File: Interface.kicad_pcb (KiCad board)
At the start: 4 copper layers, 126.6 x 95.8 mm, 92 parts, among them J101 AudioJack4, J102 switch, J3 TYPE-C-31-M-12, J4 CONN_DISPLAY, Q1 2N7002VC-7, Q2 2N7002VC-7, U1 W25Q128JVPIQ, U2 RP2040, U3 XC6210B332MR-G, Y1 12MHz

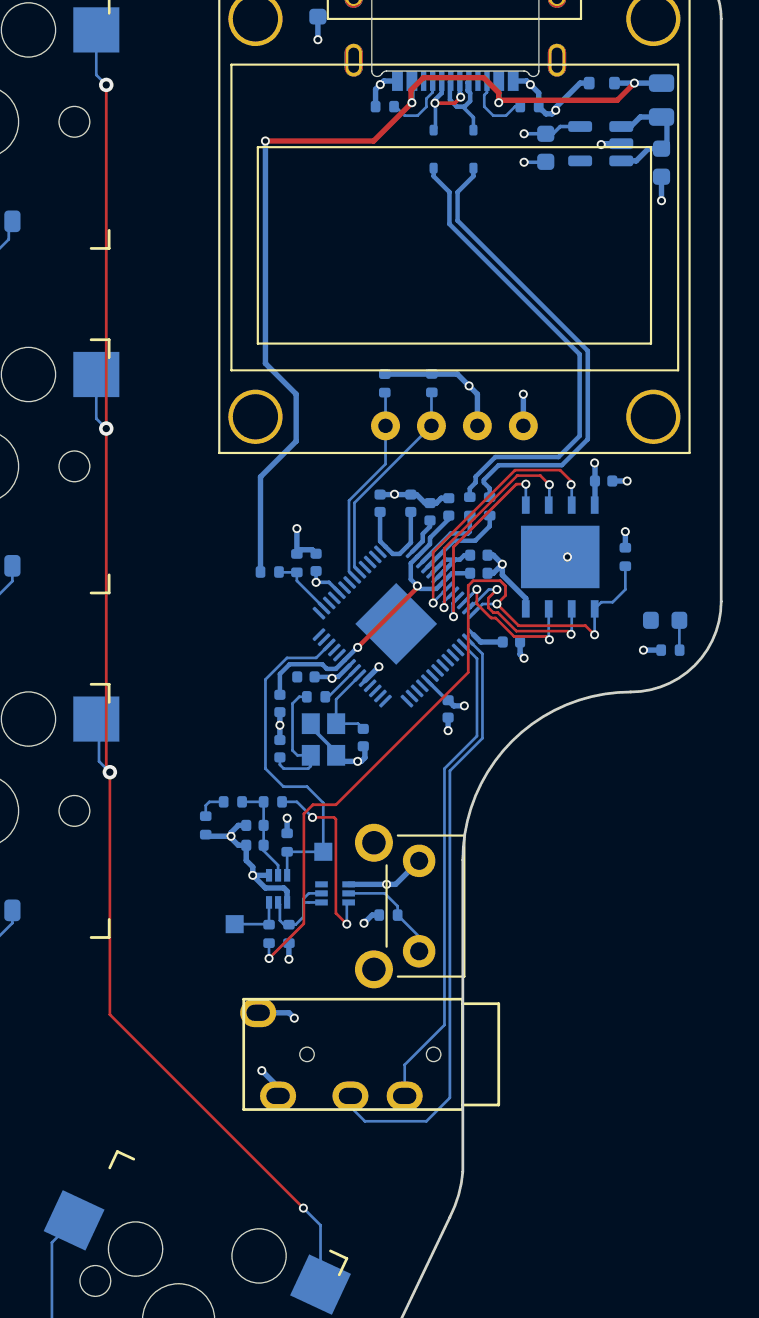
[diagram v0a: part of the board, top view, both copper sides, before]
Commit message: Add mounting holes
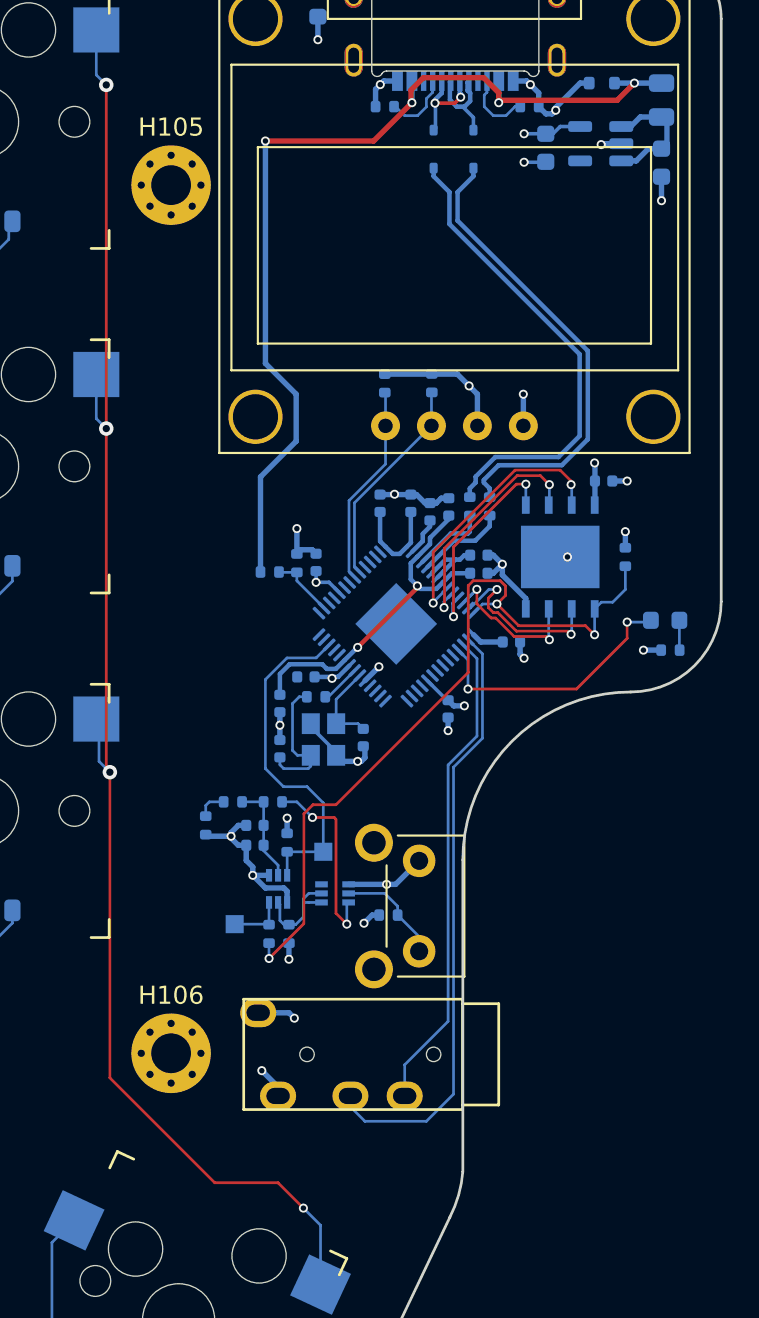
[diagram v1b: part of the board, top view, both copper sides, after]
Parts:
- added H105: MountingHole_Pad, MountingHole:MountingHole_2.2mm_M2_Pad_Via, F.Cu at (118.6, 50.9)
- added H106: MountingHole_Pad, MountingHole:MountingHole_2.2mm_M2_Pad_Via, F.Cu at (118.6, 98.9)
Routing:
- net /Left MCU/LED: track 0.00 -> 14.6 mm, vias 0 -> 2
- net /Left MCU/COL-5: track 79.7 -> 81.8 mm
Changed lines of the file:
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@@
     )
   )
+  (footprint "MountingHole:MountingHole_2.2mm_M2_Pad_Via" (layer "F.Cu")
+    (at 118.585 50.94)
+    (descr "Mounting Hole 2.2mm, M2")
+    (tags "mounting hole 2.2mm m2")
+    (property "Sheetfile" "key-matrix.kicad_sch")
+    (property "Sheetname" "Left Matrix")
+    (property "ki_description" "Mounting Hole with connection")
+    (property "ki_keywords" "mounting hole")
+    (attr exclude_from_pos_files)
+    (fp_text reference "H105" (at 0 -3.2) (layer "F.SilkS")
+        (effects (font (size 1 1) (thickness 0.15)))
+    )
+    (fp_text value "MountingHole_Pad" (at 0 3.2) (layer "F.Fab")
+        (effects (font (size 1 1) (thickness 0.15)))
+    )
+    (fp_text user "${REFERENCE}" (at 0 0) (layer "F.Fab")
+        (effects (font (size 1 1) (thickness 0.15)))
+    )
+    (fp_circle (center 0 0) (end 2.2 0)
+      (stroke (width 0.15) (type solid)) (fill none) (layer "Cmts.User"))
+    (fp_circle (center 0 0) (end 2.45 0)
+      (stroke (width 0.05) (type solid)) (fill none) (layer "F.CrtYd"))
+    (pad "1" thru_hole circle (at -1.65 0) (size 0.7 0.7) (drill 0.4) (layers "*.Cu" "*.Mask")
+      (net 2 "GND") (pinfunction "1") (pintype "input"))
+    (pad "1" thru_hole circle (at -1.166726 -1.166726) (size 0.7 0.7) (drill 0.4) (layers "*.Cu" "*.Mask")
+      (net 2 "GND") (pinfunction "1") (pintype "input"))
+    (pad "1" thru_hole circle (at -1.166726 1.166726) (size 0.7 0.7) (drill 0.4) (layers "*.Cu" "*.Mask")
+      (net 2 "GND") (pinfunction "1") (pintype "input"))
+    (pad "1" thru_hole circle (at 0 -1.65) (size 0.7 0.7) (drill 0.4) (layers "*.Cu" "*.Mask")
+      (net 2 "GND") (pinfunction "1") (pintype "input"))
+    (pad "1" thru_hole circle (at 0 0) (size 4.4 4.4) (drill 2.2) (layers "*.Cu" "*.Mask")
+      (net 2 "GND") (pinfunction "1") (pintype "input"))
+    (pad "1" thru_hole circle (at 0 1.65) (size 0.7 0.7) (drill 0.4) (layers "*.Cu" "*.Mask")
+      (net 2 "GND") (pinfunction "1") (pintype "input"))
+    (pad "1" thru_hole circle (at 1.166726 -1.166726) (size 0.7 0.7) (drill 0.4) (layers "*.Cu" "*.Mask")
+      (net 2 "GND") (pinfunction "1") (pintype "input"))
+    (pad "1" thru_hole circle (at 1.166726 1.166726) (size 0.7 0.7) (drill 0.4) (layers "*.Cu" "*.Mask")
+      (net 2 "GND") (pinfunction "1") (pintype "input"))
+    (pad "1" thru_hole circle (at 1.65 0) (size 0.7 0.7) (drill 0.4) (layers "*.Cu" "*.Mask")
+      (net 2 "GND") (pinfunction "1") (pintype "input"))
+  )
   (footprint "Keyboard:Kailh_socket_MX" (layer "F.Cu")
     (at 89.11 85.54)
@@
     )
   )
+  (footprint "MountingHole:MountingHole_2.2mm_M2_Pad_Via" (layer "F.Cu")
+    (at 118.585 98.94)
+    (descr "Mounting Hole 2.2mm, M2")
+    (tags "mounting hole 2.2mm m2")
+    (property "Sheetfile" "key-matrix.kicad_sch")
+    (property "Sheetname" "Left Matrix")
+    (property "ki_description" "Mounting Hole with connection")
+    (property "ki_keywords" "mounting hole")
+    (attr exclude_from_pos_files)
+    (fp_text reference "H106" (at 0 -3.2) (layer "F.SilkS")
+        (effects (font (size 1 1) (thickness 0.15)))
+    )
+    (fp_text value "MountingHole_Pad" (at 0 3.2) (layer "F.Fab")
+        (effects (font (size 1 1) (thickness 0.15)))
+    )
+    (fp_text user "${REFERENCE}" (at 0 0) (layer "F.Fab")
+        (effects (font (size 1 1) (thickness 0.15)))
+    )
+    (fp_circle (center 0 0) (end 2.2 0)
+      (stroke (width 0.15) (type solid)) (fill none) (layer "Cmts.User"))
+    (fp_circle (center 0 0) (end 2.45 0)
+      (stroke (width 0.05) (type solid)) (fill none) (layer "F.CrtYd"))
+    (pad "1" thru_hole circle (at -1.65 0) (size 0.7 0.7) (drill 0.4) (layers "*.Cu" "*.Mask")
+      (net 2 "GND") (pinfunction "1") (pintype "input"))
+    (pad "1" thru_hole circle (at -1.166726 -1.166726) (size 0.7 0.7) (drill 0.4) (layers "*.Cu" "*.Mask")
+      (net 2 "GND") (pinfunction "1") (pintype "input"))
+    (pad "1" thru_hole circle (at -1.166726 1.166726) (size 0.7 0.7) (drill 0.4) (layers "*.Cu" "*.Mask")
+      (net 2 "GND") (pinfunction "1") (pintype "input"))
+    (pad "1" thru_hole circle (at 0 -1.65) (size 0.7 0.7) (drill 0.4) (layers "*.Cu" "*.Mask")
+      (net 2 "GND") (pinfunction "1") (pintype "input"))
+    (pad "1" thru_hole circle (at 0 0) (size 4.4 4.4) (drill 2.2) (layers "*.Cu" "*.Mask")
+      (net 2 "GND") (pinfunction "1") (pintype "input"))
+    (pad "1" thru_hole circle (at 0 1.65) (size 0.7 0.7) (drill 0.4) (layers "*.Cu" "*.Mask")
+      (net 2 "GND") (pinfunction "1") (pintype "input"))
+    (pad "1" thru_hole circle (at 1.166726 -1.166726) (size 0.7 0.7) (drill 0.4) (layers "*.Cu" "*.Mask")
+      (net 2 "GND") (pinfunction "1") (pintype "input"))
+    (pad "1" thru_hole circle (at 1.166726 1.166726) (size 0.7 0.7) (drill 0.4) (layers "*.Cu" "*.Mask")
+      (net 2 "GND") (pinfunction "1") (pintype "input"))
+    (pad "1" thru_hole circle (at 1.65 0) (size 0.7 0.7) (drill 0.4) (layers "*.Cu" "*.Mask")
+      (net 2 "GND") (pinfunction "1") (pintype "input"))
+  )
   (footprint "Keyboard:Kailh_socket_MX" (layer "F.Cu")
     (at 70.06 79.54)
@@
   (segment (start 128.919369 80.715843) (end 129.209369 81.005843) (width 0.15) (layer "B.Cu") (net 28))
   (segment (start 127.709369 80.715843) (end 127.709369 79.370531) (width 0.15) (layer "B.Cu") (net 28))
+  (segment (start 141 78.8) (end 143.8 76) (width 0.15) (layer "F.Cu") (net 29))
+  (segment (start 143.8 76) (end 143.8 75.1) (width 0.15) (layer "F.Cu") (net 29))
+  (segment (start 135 78.8) (end 141 78.8) (width 0.15) (layer "F.Cu") (net 29))
+  (via (at 143.8 75.1) (size 0.5) (drill 0.3) (layers "F.Cu" "B.Cu") (net 29))
+  (via (at 135 78.8) (size 0.5) (drill 0.3) (layers "F.Cu" "B.Cu") (net 29))
+  (segment (start 145.0125 75.1) (end 145.1125 75) (width 0.15) (layer "B.Cu") (net 29))
+  (segment (start 135 77.18873) (end 135 78.8) (width 0.15) (layer "B.Cu") (net 29))
+  (segment (start 134.452 76.64073) (end 135 77.18873) (width 0.15) (layer "B.Cu") (net 29))
+  (segment (start 143.8 75.1) (end 145.0125 75.1) (width 0.15) (layer "B.Cu") (net 29))
   (segment (start 133.1745 46.408352) (end 134.264435 46.408352) (width 0.2) (layer "F.Cu") (net 30))
   (segment (start 134.264435 46.408352) (end 134.59479 46.077997) (width 0.2) (layer "F.Cu") (net 30))
@@
   (segment (start 140.7 67.5) (end 140.735 67.535) (width 0.15) (layer "B.Cu") (net 44))
   (segment (start 140.735 67.535) (end 140.735 68.6298) (width 0.15) (layer "B.Cu") (net 44))
+  (segment (start 135.8 76.85736) (end 135.8 81.524264) (width 0.15) (layer "B.Cu") (net 45))
+  (segment (start 128.5 101.9) (end 128.5 101.3) (width 0.15) (layer "B.Cu") (net 45))
   (segment (start 135.017685 76.075045) (end 135.8 76.85736) (width 0.15) (layer "B.Cu") (net 45))
-  (segment (start 134 101.4) (end 132.7 102.7) (width 0.15) (layer "B.Cu") (net 45))
   (segment (start 132.7 102.7) (end 129.3 102.7) (width 0.15) (layer "B.Cu") (net 45))
+  (segment (start 134.2 101.2) (end 132.7 102.7) (width 0.15) (layer "B.Cu") (net 45))
+  (segment (start 134.2 83.124264) (end 134.2 101.2) (width 0.15) (layer "B.Cu") (net 45))
   (segment (start 129.3 102.7) (end 128.5 101.9) (width 0.15) (layer "B.Cu") (net 45))
-  (segment (start 135.8 81.524264) (end 134 83.324264) (width 0.15) (layer "B.Cu") (net 45))
-  (segment (start 135.8 76.85736) (end 135.8 81.524264) (width 0.15) (layer "B.Cu") (net 45))
-  (segment (start 134 83.324264) (end 134 101.4) (width 0.15) (layer "B.Cu") (net 45))
-  (segment (start 128.5 101.9) (end 128.5 101.3) (width 0.15) (layer "B.Cu") (net 45))
+  (segment (start 135.8 81.524264) (end 134.2 83.124264) (width 0.15) (layer "B.Cu") (net 45))
+  (segment (start 133.9 83) (end 133.9 97.174695) (width 0.15) (layer "B.Cu") (net 46))
+  (segment (start 135.5 77.123044) (end 135.5 81.4) (width 0.15) (layer "B.Cu") (net 46))
   (segment (start 131.5 99.574695) (end 131.5 101.3) (width 0.15) (layer "B.Cu") (net 46))
+  (segment (start 135.5 81.4) (end 133.9 83) (width 0.15) (layer "B.Cu") (net 46))
   (segment (start 134.734843 76.357887) (end 135.5 77.123044) (width 0.15) (layer "B.Cu") (net 46))
-  (segment (start 135.5 81.4) (end 133.7 83.2) (width 0.15) (layer "B.Cu") (net 46))
-  (segment (start 135.5 77.123044) (end 135.5 81.4) (width 0.15) (layer "B.Cu") (net 46))
-  (segment (start 133.7 83.2) (end 133.7 97.374695) (width 0.15) (layer "B.Cu") (net 46))
-  (segment (start 133.7 97.374695) (end 131.5 99.574695) (width 0.15) (layer "B.Cu") (net 46))
+  (segment (start 133.9 97.174695) (end 131.5 99.574695) (width 0.15) (layer "B.Cu") (net 46))
   (segment (start 120.65 119.975) (end 120.65 119.175) (width 0.15) (layer "B.Cu") (net 47))
   (segment (start 110.575 121.375) (end 119.25 121.375) (width 0.15) (layer "B.Cu") (net 47))
@@
   (segment (start 96 83.2) (end 95.6 82.8) (width 0.15) (layer "B.Cu") (net 55))
   (segment (start 115.2 83.4) (end 115 83.2) (width 0.15) (layer "F.Cu") (net 56))
+  (segment (start 121 106.1) (end 115.2 100.3) (width 0.15) (layer "F.Cu") (net 56))
+  (segment (start 115.2 100.3) (end 115.2 83.4) (width 0.15) (layer "F.Cu") (net 56))
   (segment (start 115 83.2) (end 115 64.4) (width 0.15) (layer "F.Cu") (net 56))
-  (segment (start 115.2 96.8) (end 115.2 83.4) (width 0.15) (layer "F.Cu") (net 56))
   (segment (start 115 64.4) (end 115 45.4) (width 0.15) (layer "F.Cu") (net 56))
-  (segment (start 125.9 107.5) (end 115.2 96.8) (width 0.15) (layer "F.Cu") (net 56))
+  (segment (start 124.5 106.1) (end 121 106.1) (width 0.15) (layer "F.Cu") (net 56))
+  (segment (start 125.9 107.5) (end 124.5 106.1) (width 0.15) (layer "F.Cu") (net 56))
   (via (at 115 45.4) (size 0.8) (drill 0.4) (layers "F.Cu" "B.Cu") (net 56))
   (via (at 115 64.4) (size 0.8) (drill 0.4) (layers "F.Cu" "B.Cu") (net 56))

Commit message: remove backups
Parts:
- moved R11 0.62 mm to (124.2, 71.8), turned to -90 degrees
- moved C8 0.16 mm to (126.8, 71.8)
- moved U3 0.13 mm to (142.2, 48.8)
- moved R12 0.10 mm to (125.5, 71.8)
- moved C16 0.05 mm to (139.2, 48.9)
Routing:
- net /Left MCU/ROW-4: track 26.0 -> 84.7 mm
- net VBUS: track 54.1 -> 52.7 mm
- net GND: track 53.6 -> 52.6 mm, vias 23 -> 22
- net +3V3: track 39.2 -> 39.9 mm
- net /Left MCU/QSPI_SCLK: track 13.1 -> 13.7 mm
- net /Left MCU/QSPI_SD0: track 11.6 -> 12.2 mm

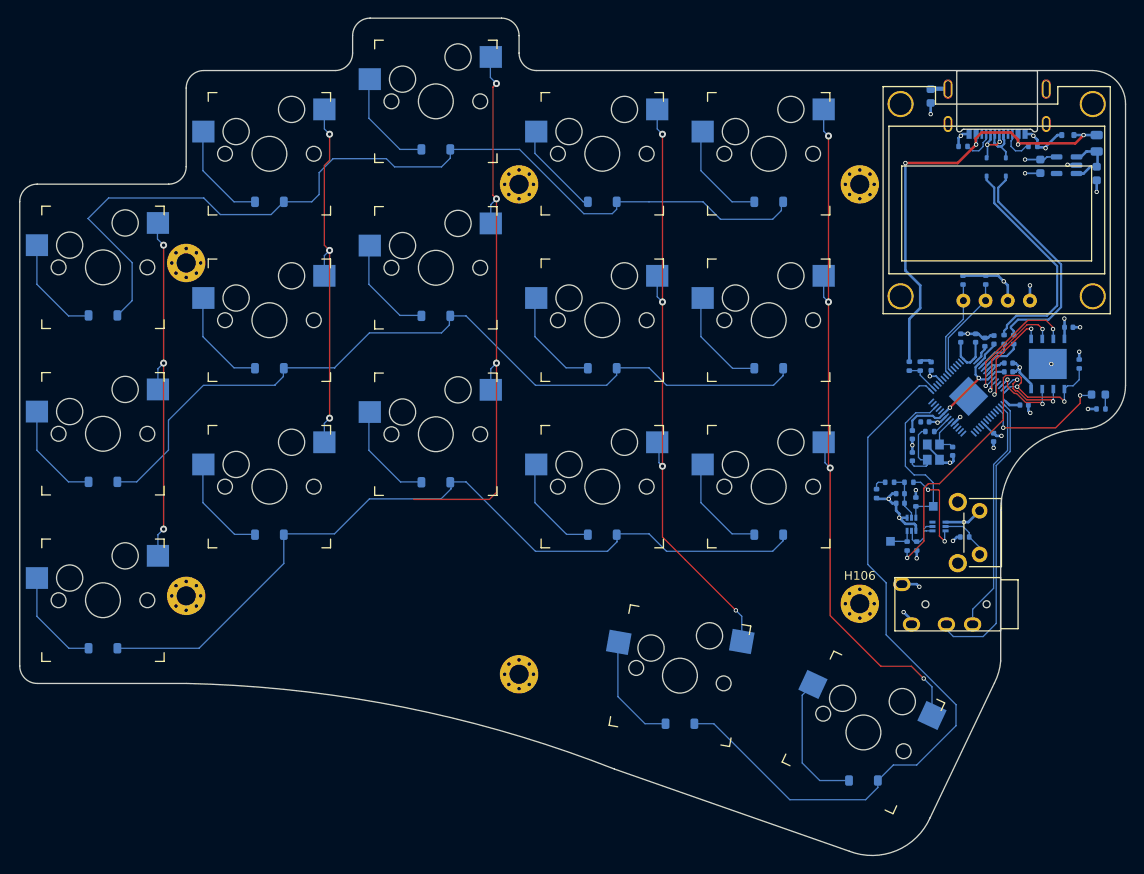
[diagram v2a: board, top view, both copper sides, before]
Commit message: Cleanup routing
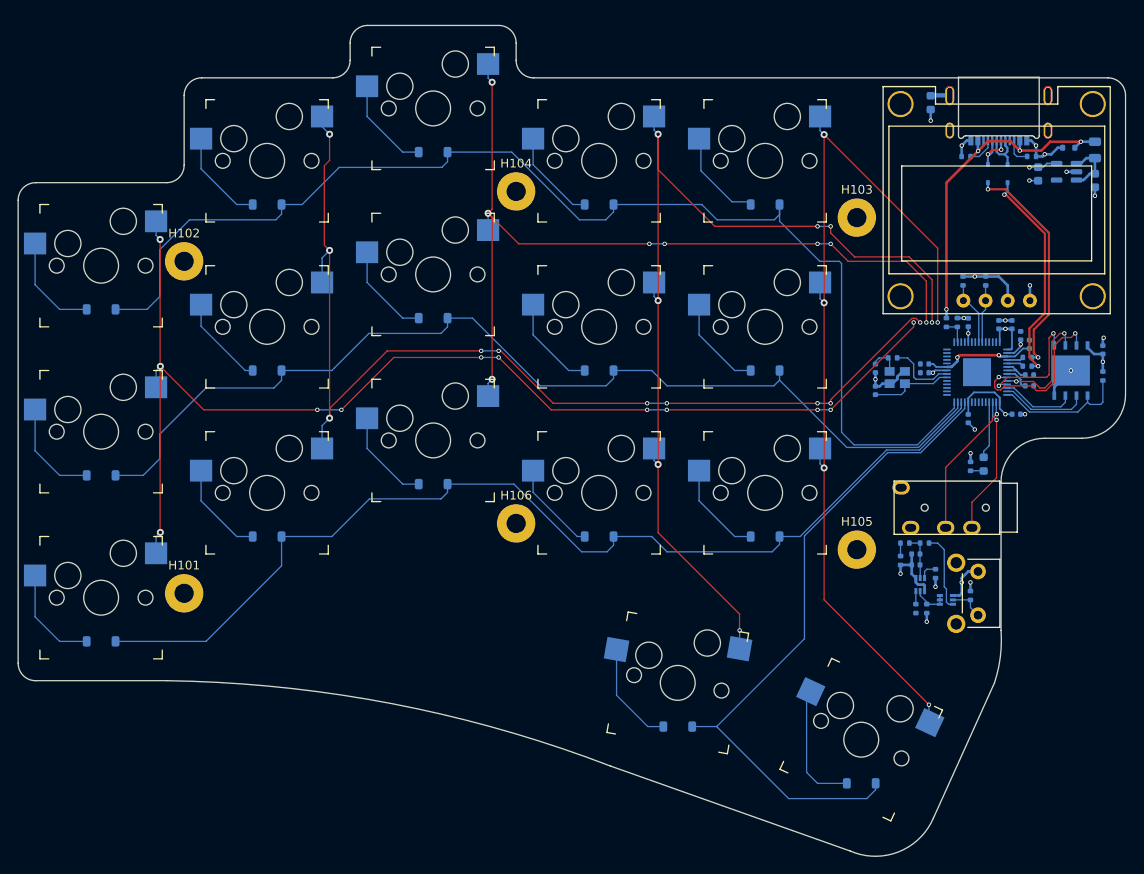
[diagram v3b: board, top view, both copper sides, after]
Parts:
- removed TP1: RESET, TestPoint:TestPoint_Pad_1.0x1.0mm
- removed TP2: BOOTSEL, TestPoint:TestPoint_Pad_1.0x1.0mm
- H101, H102, H103, H104, H105, H106: footprint MountingHole:MountingHole_2.2mm_M2_Pad_Via -> MountingHole:MountingHole_2.2mm_M2_Pad
- moved H104 55.3 mm to (79.2, 51.8)
- moved H105 41.8 mm to (118.2, 92.8)
- moved H106 40.4 mm to (79.2, 89.8)
- moved H103 38.9 mm to (118.2, 54.8)
- moved R1 16.3 mm to (131.3, 83.2), turned to -90 degrees
- moved D1 15.4 mm to (132.8, 83.0), turned to 90 degrees
- moved C2 11.2 mm to (120.4, 74.5), turned to 90 degrees
- moved J101 11.1 mm to (134.6, 88.0)
- moved C3 10.9 mm to (120.4, 72.0), turned to -90 degrees
- moved Y1 9.49 mm to (122.9, 73.0), turned to 0 degrees
- moved R3 9.44 mm to (122.3, 70.8)
- moved R13 8.51 mm to (127.2, 95.5), turned to 90 degrees
- moved Q1 8.44 mm to (128.5, 98.5)
- moved C13 8.22 mm to (126.0, 71.5), turned to 180 degrees
- moved R16 8.14 mm to (123.2, 94.0)
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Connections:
- net Net-(Q2B-D) renamed /Left MCU/~{BOOTSEL}
- U2 pad 11: unconnected-(U2-GPIO8-Pad11) -> /Left MCU/ROW-4
- U2 pad 12: /Left MCU/ROW-1 -> /Left MCU/ROW-3
- U2 pad 14: /Left MCU/ROW-3 -> /Left MCU/ROW-1
- U2 pad 29: /Left MCU/ROW-4 -> unconnected-(U2-GPIO18-Pad29)
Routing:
- net /Left MCU/COL-1: track 42.0 -> 139.1 mm, vias 3 -> 12
- net /Left MCU/COL-2: track 42.3 -> 121.6 mm, vias 3 -> 10
- net /Left MCU/COL-4: track 70.8 -> 115.2 mm, vias 4 -> 7
- net /Left MCU/ROW-1: track 107.3 -> 140.8 mm
- net /Left MCU/COL-3: track 66.0 -> 99.0 mm, vias 3 -> 8
- net /Left MCU/QSPI_~{CS}: track 42.7 -> 15.7 mm, vias 3 -> 0
- net /Left MCU/ROW-3: track 93.2 -> 120.1 mm
- net /Left MCU/ROW-2: track 94.2 -> 119.0 mm
- net /Left MCU/COL-5: track 81.8 -> 106.4 mm, vias 4 -> 5
- net /Left MCU/~{RESET}: track 19.2 -> 2.11 mm
- net /Left MCU/TX: track 33.4 -> 16.9 mm, vias 0 -> 1
- net VBUS: track 52.7 -> 38.6 mm
- net /Left MCU/RX: track 26.9 -> 15.7 mm, vias 0 -> 1
- net GND: track 52.6 -> 42.8 mm, vias 22 -> 18
- net /Left MCU/ROW-4: track 84.7 -> 76.7 mm
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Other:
- board size 126.6 x 95.8 mm -> 126.8 x 95.1 mm
